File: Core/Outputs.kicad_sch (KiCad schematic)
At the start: 65 parts, among them J3 Conn_01x10_Female, J7 Conn_01x10_Female, Q14 2N7002, U10 TL072, U11 TL072, U12 TL072, U15 MAX5134, U2 TMUX4052, U4 TL072, U5 TL072, U6 TL072, U7 TL072, U8 TMUX4052, U9 TL072

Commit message: Finalize module
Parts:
- U2, U8: value TMUX4052 -> MC74LVXT4052
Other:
- note added: "Beware! Logic on voltage must be below 3.3V Logic levels are not compatible on most 4052 variations. TMUX4052 or MC74LVXT4052 are compatible"
- note removed: "Do not use CD4052! Logic levels are not compatible"
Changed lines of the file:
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@@
     (stroke (width 0) (type default))
   )
-  (text "Do not use CD4052!\nLogic levels are not compatible"
-    (at 105.41 158.115 0)
+  (text "Beware! Logic on voltage must be below 3.3V\nLogic levels are not compatible on most 4052 variations.\nTMUX4052 or MC74LVXT4052 are compatible"
+    (at 81.28 156.845 0)
     (effects (font (size 1.27 1.27)) (justify left bottom))
   )
@@
       (effects (font (size 1.27 1.27)))
     )
-    (property "Value" "TMUX4052" (at 288.925 166.624 0)
+    (property "Value" "MC74LVXT4052" (at 288.925 166.624 0)
       (effects (font (size 1.27 1.27)))
     )
@@
       (effects (font (size 1.27 1.27)) (justify left) hide)
     )
-    (property "Datasheet" "http://www.ti.com/lit/ds/symlink/tl071.pdf" (at 288.417 181.61 0)
+    (property "Datasheet" "https://no.mouser.com/datasheet/2/308/1/MC74LVXT4052_D-2315524.pdf" (at 288.417 181.61 0)
       (effects (font (size 1.27 1.27)) hide)
     )
@@
       (effects (font (size 1.27 1.27)))
     )
-    (property "Value" "TMUX4052" (at 140.97 166.624 0)
+    (property "Value" "MC74LVXT4052" (at 140.97 166.624 0)
       (effects (font (size 1.27 1.27)))
     )
@@
       (effects (font (size 1.27 1.27)) (justify left) hide)
     )
-    (property "Datasheet" "http://www.ti.com/lit/ds/symlink/tl071.pdf" (at 140.462 181.61 0)
+    (property "Datasheet" "https://no.mouser.com/datasheet/2/308/1/MC74LVXT4052_D-2315524.pdf" (at 140.462 181.61 0)
       (effects (font (size 1.27 1.27)) hide)
     )

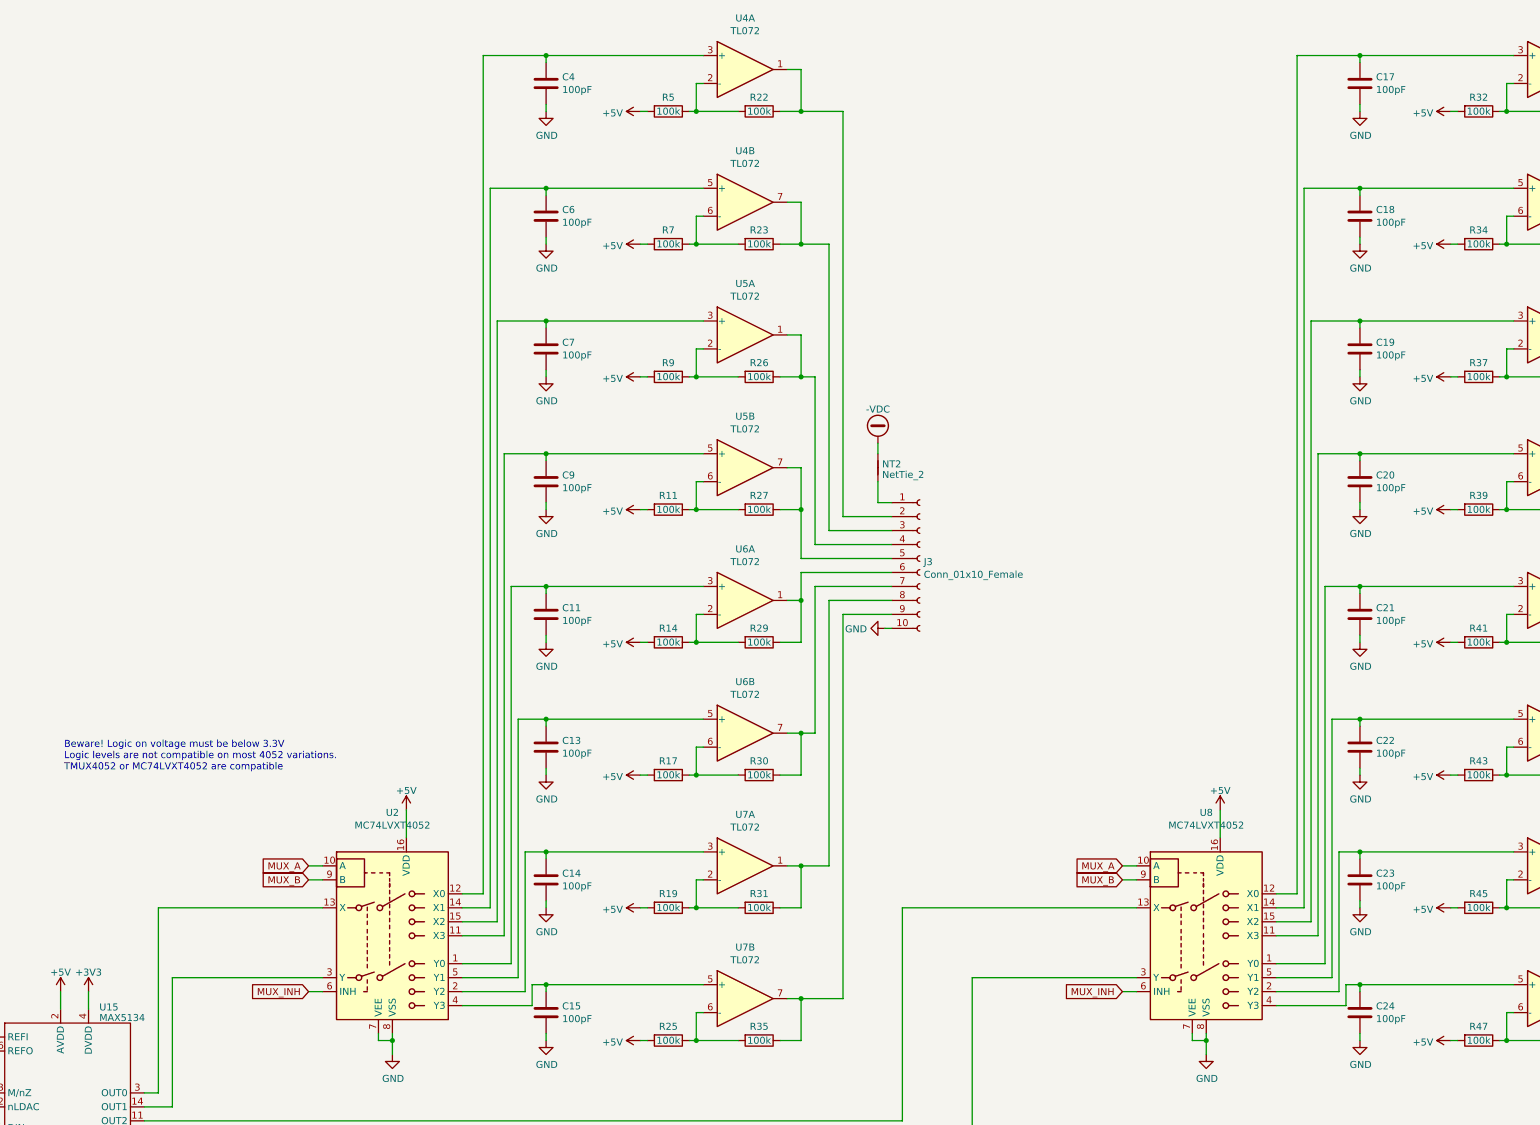
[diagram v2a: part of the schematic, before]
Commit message: Specify dielectric type of SnH caps
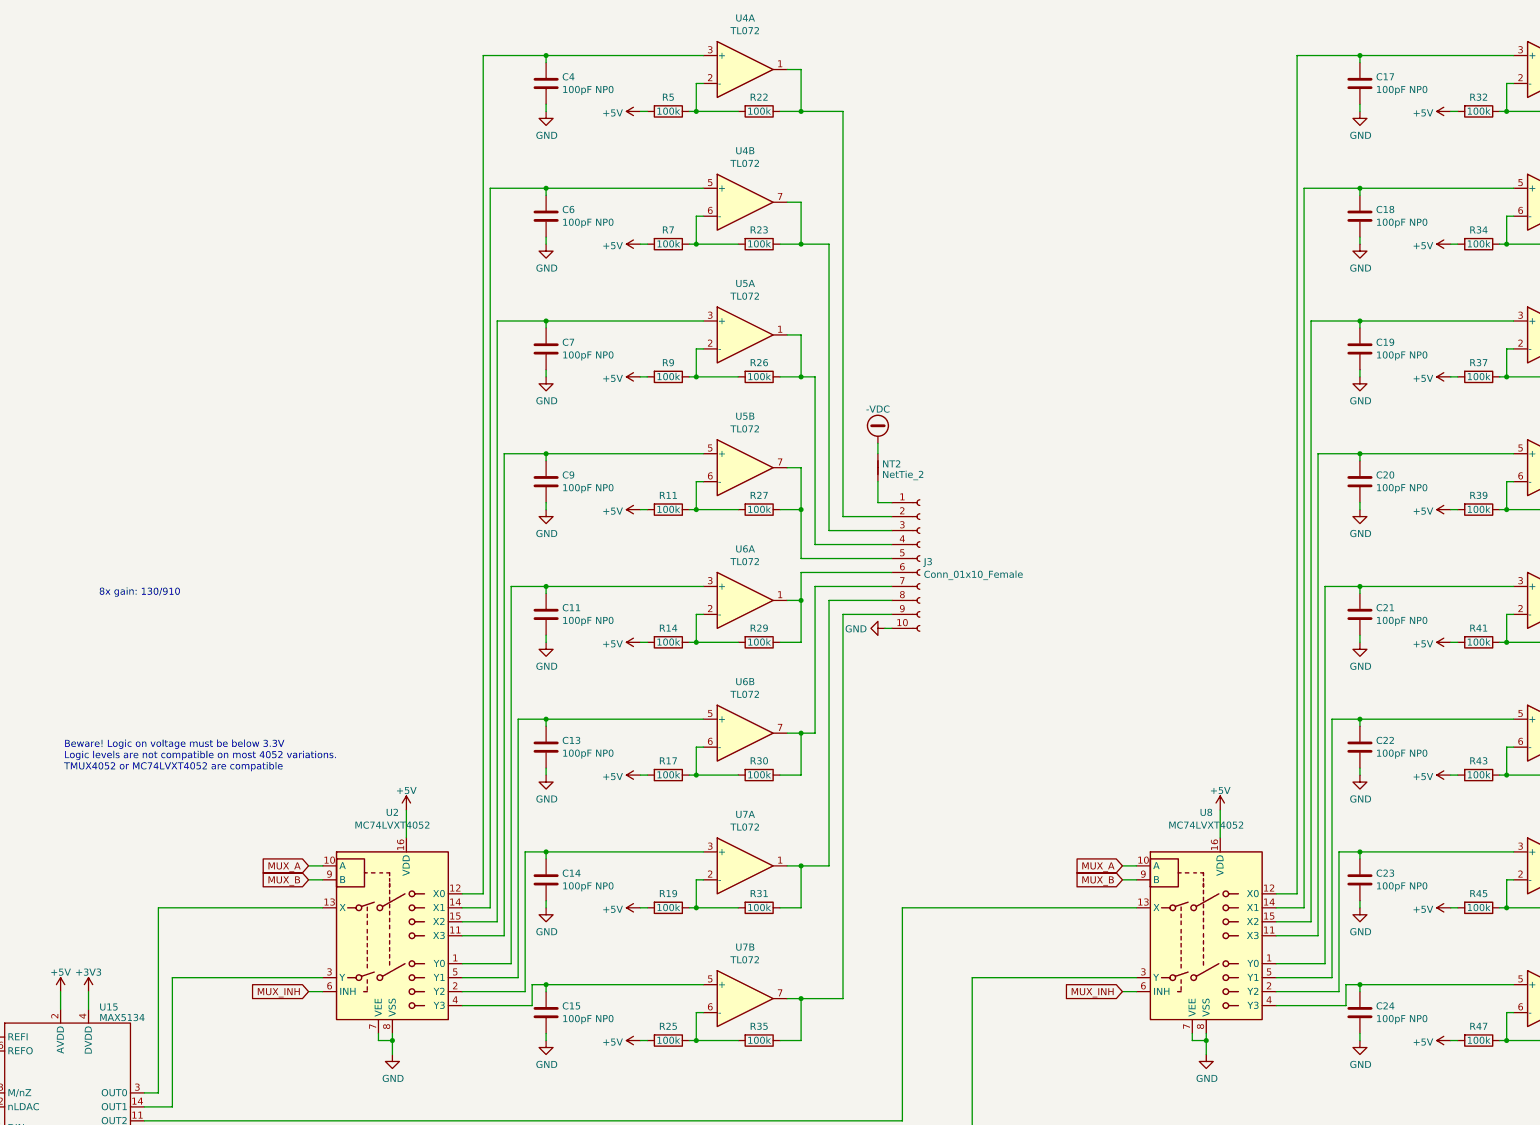
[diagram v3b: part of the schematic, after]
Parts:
- C11, C13, C14, C15, C17, C18, C19, C20, C21, C22, C23, C24, C4, C6, C7, C9: value 100pF -> 100pF NP0
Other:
- note added: "8x gain: 130/910"
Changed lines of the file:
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@@
     (stroke (width 0) (type default))
   )
+  (text "8x gain: 130/910" (at 87.63 125.095 0)
+    (effects (font (size 1.27 1.27)) (justify left bottom))
+  )
   (text "Beware! Logic on voltage must be below 3.3V\nLogic levels are not compatible on most 4052 variations.\nTMUX4052 or MC74LVXT4052 are compatible"
     (at 81.28 156.845 0)
@@
       (effects (font (size 1.27 1.27)) (justify left))
     )
-    (property "Value" "100pF" (at 171.831 201.803 0)
+    (property "Value" "100pF NP0" (at 171.831 201.803 0)
       (effects (font (size 1.27 1.27)) (justify left))
     )
@@
       (effects (font (size 1.27 1.27)) (justify left))
     )
-    (property "Value" "100pF" (at 171.831 105.283 0)
+    (property "Value" "100pF NP0" (at 171.831 105.283 0)
       (effects (font (size 1.27 1.27)) (justify left))
     )
@@
       (effects (font (size 1.27 1.27)) (justify left))
     )
-    (property "Value" "100pF" (at 319.786 153.543 0)
+    (property "Value" "100pF NP0" (at 319.786 153.543 0)
       (effects (font (size 1.27 1.27)) (justify left))
     )
@@
       (effects (font (size 1.27 1.27)) (justify left))
     )
-    (property "Value" "100pF" (at 171.831 129.413 0)
+    (property "Value" "100pF NP0" (at 171.831 129.413 0)
       (effects (font (size 1.27 1.27)) (justify left))
     )
@@
       (effects (font (size 1.27 1.27)) (justify left))
     )
-    (property "Value" "100pF" (at 171.831 153.543 0)
+    (property "Value" "100pF NP0" (at 171.831 153.543 0)
       (effects (font (size 1.27 1.27)) (justify left))
     )
@@
       (effects (font (size 1.27 1.27)) (justify left))
     )
-    (property "Value" "100pF" (at 319.786 32.893 0)
+    (property "Value" "100pF NP0" (at 319.786 32.893 0)
       (effects (font (size 1.27 1.27)) (justify left))
     )
@@
       (effects (font (size 1.27 1.27)) (justify left))
     )
-    (property "Value" "100pF" (at 171.831 32.893 0)
+    (property "Value" "100pF NP0" (at 171.831 32.893 0)
       (effects (font (size 1.27 1.27)) (justify left))
     )
@@
       (effects (font (size 1.27 1.27)) (justify left))
     )
-    (property "Value" "100pF" (at 171.831 177.673 0)
+    (property "Value" "100pF NP0" (at 171.831 177.673 0)
       (effects (font (size 1.27 1.27)) (justify left))
     )
@@
       (effects (font (size 1.27 1.27)) (justify left))
     )
-    (property "Value" "100pF" (at 171.831 81.153 0)
+    (property "Value" "100pF NP0" (at 171.831 81.153 0)
       (effects (font (size 1.27 1.27)) (justify left))
     )
@@
       (effects (font (size 1.27 1.27)) (justify left))
     )
-    (property "Value" "100pF" (at 319.786 177.673 0)
+    (property "Value" "100pF NP0" (at 319.786 177.673 0)
       (effects (font (size 1.27 1.27)) (justify left))
     )
@@
       (effects (font (size 1.27 1.27)) (justify left))
     )
-    (property "Value" "100pF" (at 319.786 201.803 0)
+    (property "Value" "100pF NP0" (at 319.786 201.803 0)
       (effects (font (size 1.27 1.27)) (justify left))
     )
@@
       (effects (font (size 1.27 1.27)) (justify left))
     )
-    (property "Value" "100pF" (at 319.786 81.153 0)
+    (property "Value" "100pF NP0" (at 319.786 81.153 0)
       (effects (font (size 1.27 1.27)) (justify left))
     )
@@
       (effects (font (size 1.27 1.27)) (justify left))
     )
-    (property "Value" "100pF" (at 319.786 105.283 0)
+    (property "Value" "100pF NP0" (at 319.786 105.283 0)
       (effects (font (size 1.27 1.27)) (justify left))
     )
@@
       (effects (font (size 1.27 1.27)) (justify left))
     )
-    (property "Value" "100pF" (at 319.786 57.023 0)
+    (property "Value" "100pF NP0" (at 319.786 57.023 0)
       (effects (font (size 1.27 1.27)) (justify left))
     )
@@
       (effects (font (size 1.27 1.27)) (justify left))
     )
-    (property "Value" "100pF" (at 171.831 57.023 0)
+    (property "Value" "100pF NP0" (at 171.831 57.023 0)
       (effects (font (size 1.27 1.27)) (justify left))
     )
@@
       (effects (font (size 1.27 1.27)) (justify left))
     )
-    (property "Value" "100pF" (at 319.786 129.413 0)
+    (property "Value" "100pF NP0" (at 319.786 129.413 0)
       (effects (font (size 1.27 1.27)) (justify left))
     )

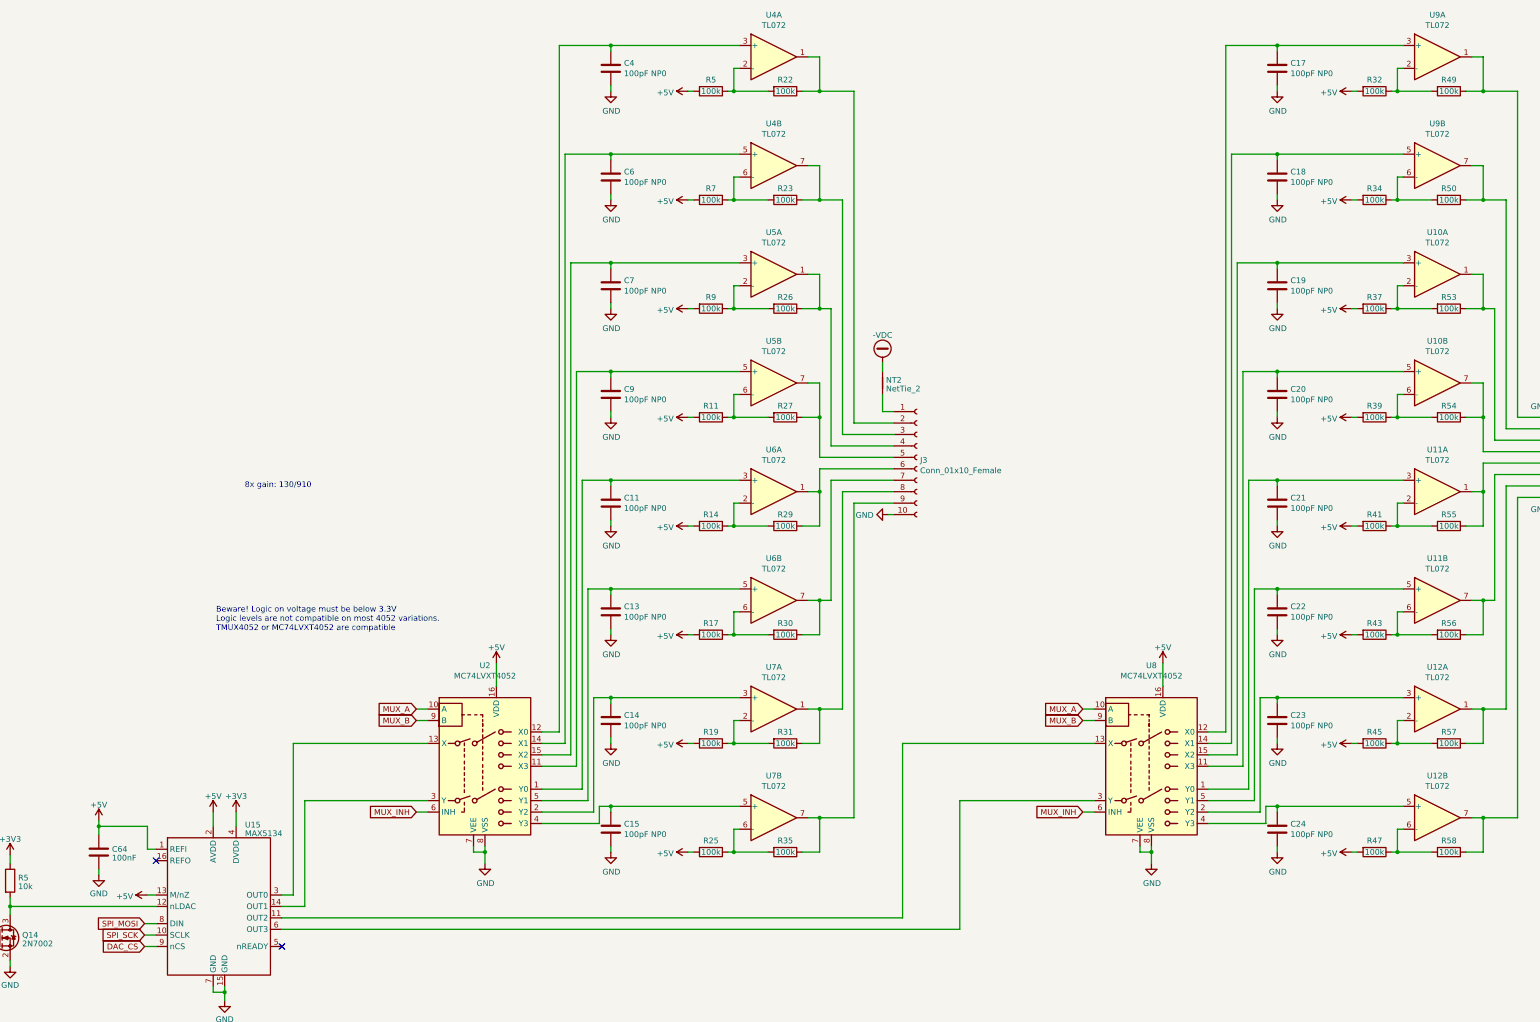
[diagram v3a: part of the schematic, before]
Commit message: Change SPI bus for EEPROM
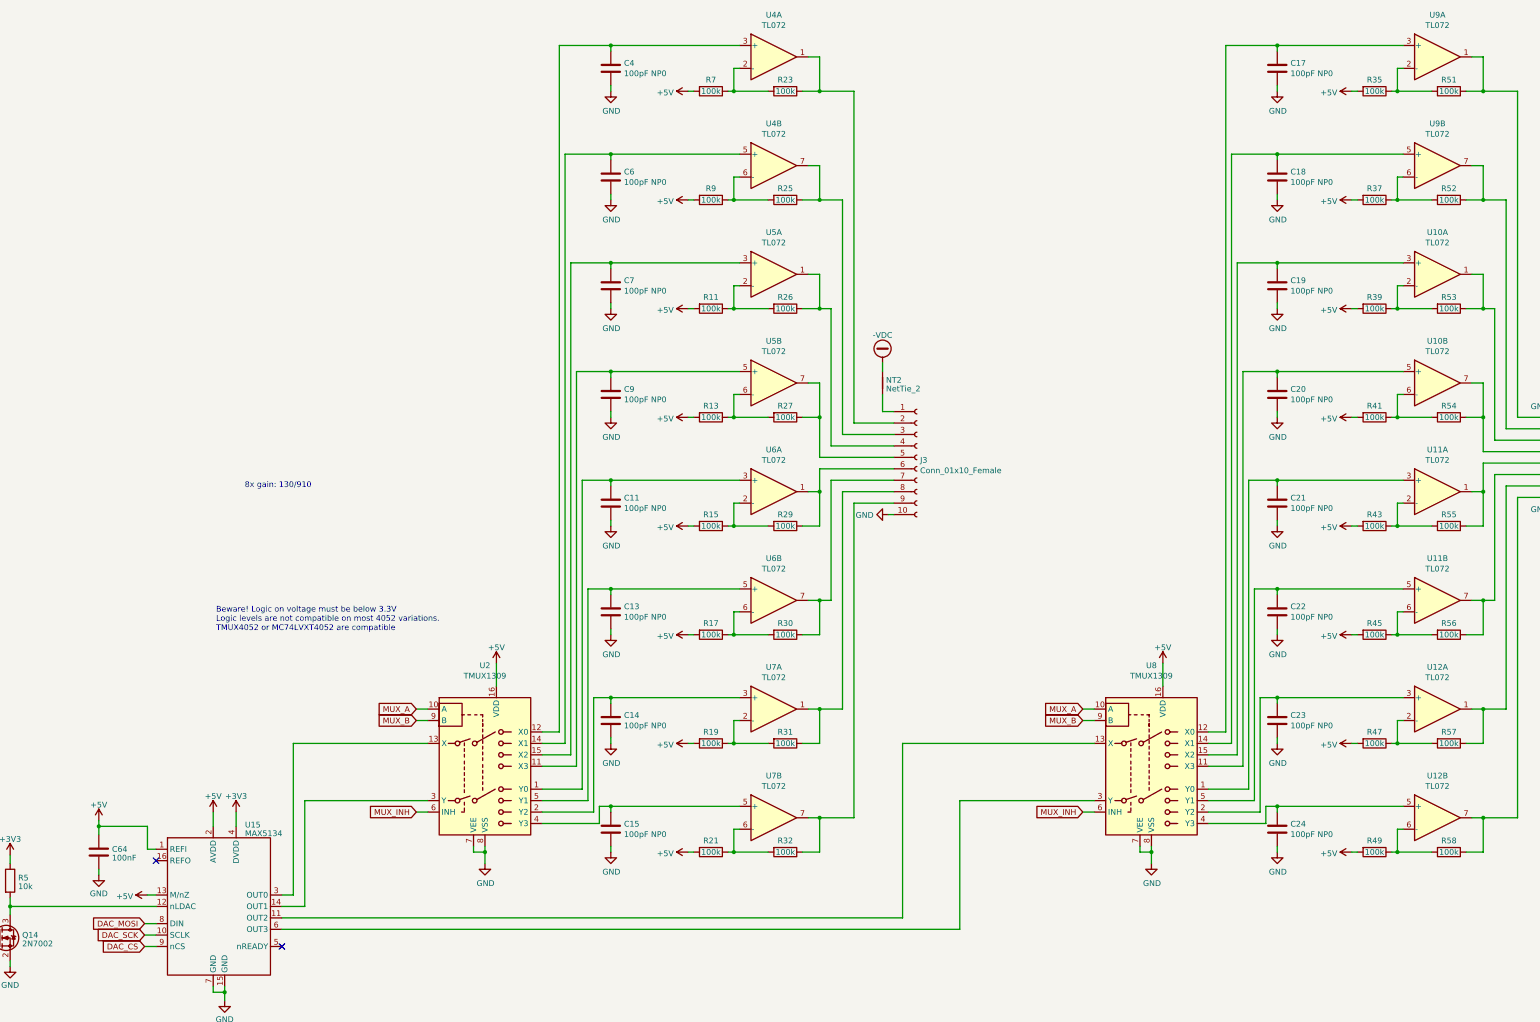
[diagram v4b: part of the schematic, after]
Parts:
- U2, U8: value MC74LVXT4052 -> TMUX1309; footprint Package_SO:SOIC-16_3.9x9.9mm_P1.27mm -> Package_SO:TSSOP-16_4.4x5mm_P0.65mm
- renumbered R9 to R11, R11 to R13, R14 to R15, R25 to R21, R22 to R23, R23 to R25, R35 to R32, R32 to R35, R34 to R37, R37 to R39, R39 to R41, R41 to R43, R43 to R45, R45 to R47, R47 to R49, R49 to R51, R50 to R52, R5 to R7, R7 to R9
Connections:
- net SPI_MOSI renamed DAC_MOSI
- net SPI_SCK renamed DAC_SCK
